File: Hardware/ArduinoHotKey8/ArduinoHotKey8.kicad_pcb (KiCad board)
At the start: 2 copper layers, 96.5 x 77.5 mm, 38 parts, among them SW0 SW_Push, SW1 SW_Push, SW2 SW_Push, SW3 SW_Push, SW4 SW_Push, SW5 SW_Push, SW6 SW_Push, SW7 SW_Push

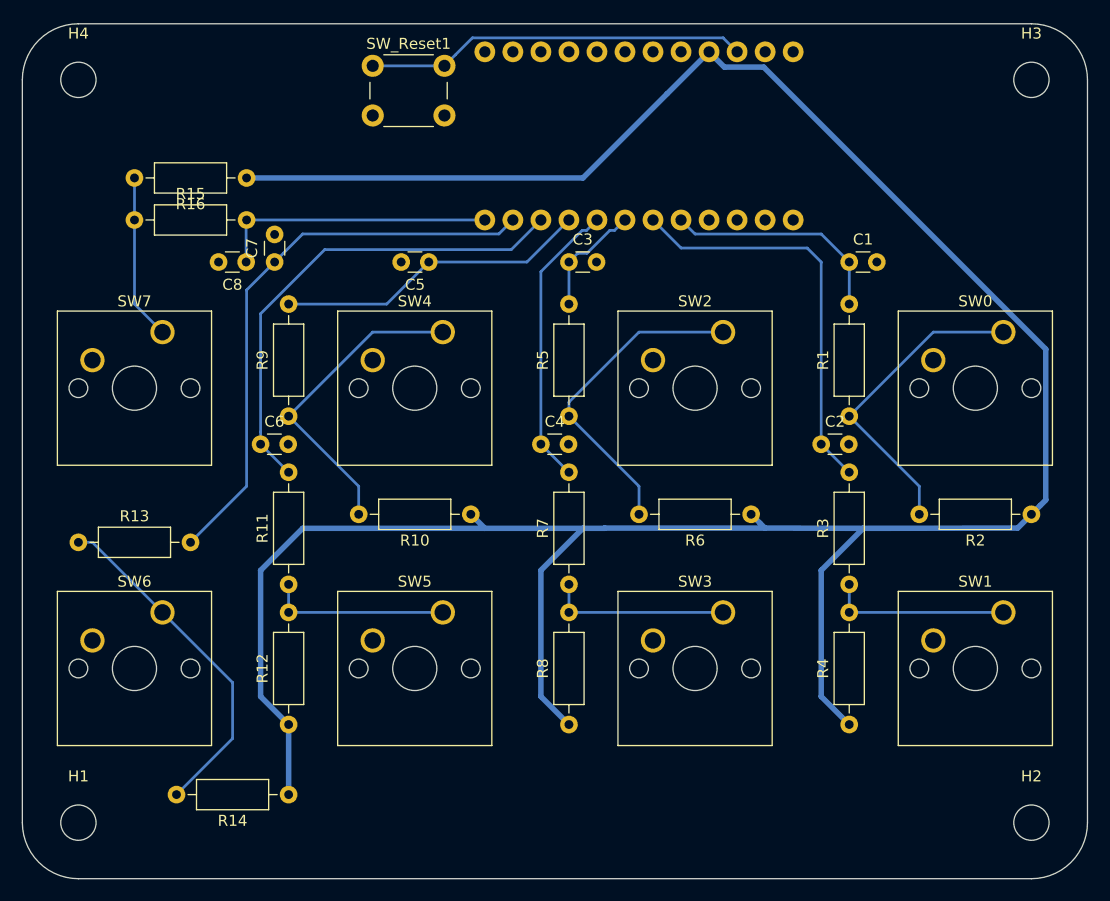
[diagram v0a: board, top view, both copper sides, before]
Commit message: Update ArduinoHotKey8.kicad_pcb
Fixed missing infill
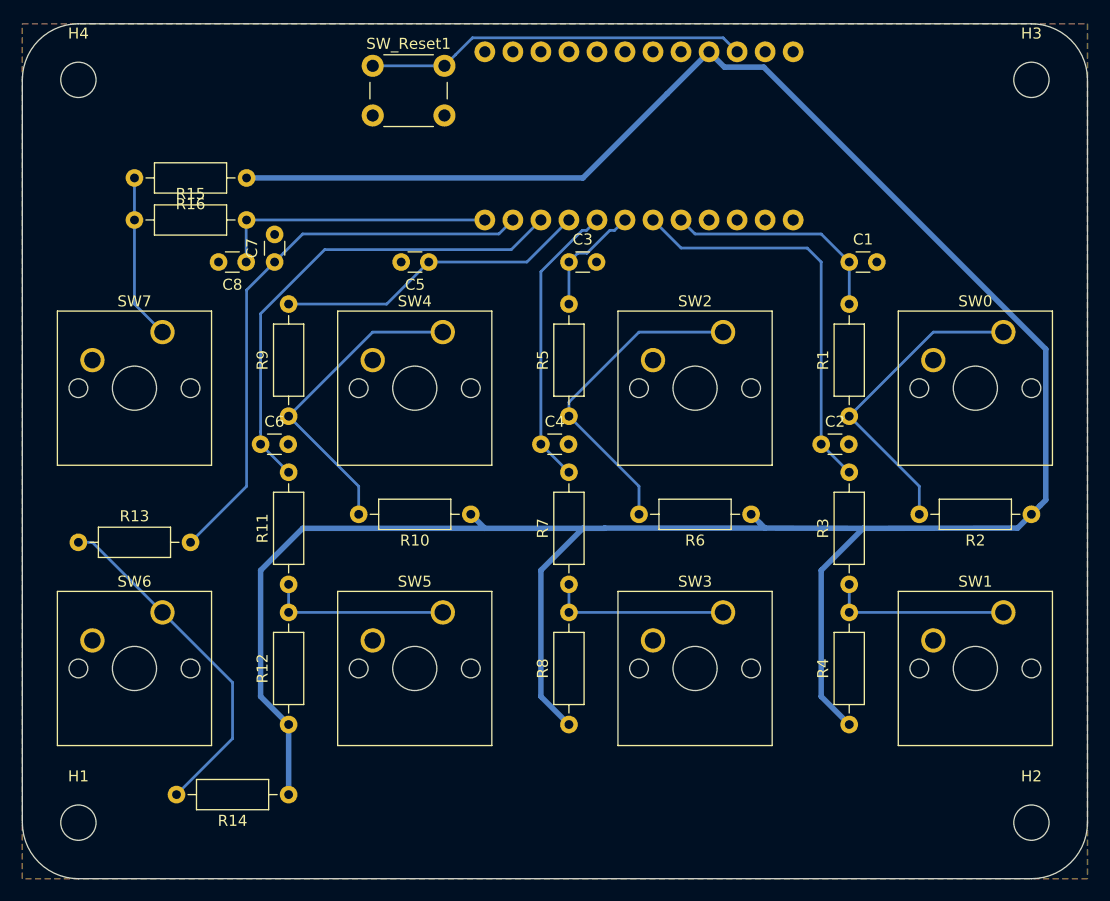
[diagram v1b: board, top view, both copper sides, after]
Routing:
- added copper zone on B.Cu, net GND
- added copper zone on F.Cu, net GND
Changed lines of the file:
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@@
     (solder_mask_min_width 0.25)
     (aux_axis_origin 0 0)
-    (visible_elements FFFFFF7F)
+    (visible_elements 7FFFFFFF)
     (pcbplotparams
       (layerselection 0x010fc_ffffffff)
@@
   (segment (start 30.48 45.72) (end 33.02 48.26) (width 0.25) (layer B.Cu) (net 19))
   (segment (start 30.48 38.1) (end 30.48 45.72) (width 0.25) (layer B.Cu) (net 19))
+  (zone (net 1) (net_name GND) (layer F.Cu) (hatch edge 0.508)
+    (connect_pads (clearance 0.508))
+    (min_thickness 0.254)
+    (fill yes (arc_segments 32) (thermal_gap 0.508) (thermal_bridge_width 0.508))
+    (polygon
+      (pts
+        (xy 116.84 97.79) (xy 20.32 97.79) (xy 20.32 20.32) (xy 116.84 20.32)
+      )
+    )
+  )
+  (zone (net 1) (net_name GND) (layer B.Cu) (hatch edge 0.508)
+    (connect_pads (clearance 0.508))
+    (min_thickness 0.254)
+    (fill yes (arc_segments 32) (thermal_gap 0.508) (thermal_bridge_width 0.508))
+    (polygon
+      (pts
+        (xy 116.84 97.79) (xy 20.32 97.79) (xy 20.32 20.32) (xy 116.84 20.32)
+      )
+    )
+  )
 )

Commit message: Added ISP Header
Added ISP Header and moved bulky parts to the back
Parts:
- added J1: AVR-ISP-6, Connector_IDC:IDC-Header_2x03_P2.54mm_Vertical, B.Cu at (39.4, 25.4)
- SW_Reset1: moved to B.Cu
- moved SW_Reset1 6.35 mm to (58.4, 24.1), turned to 180 degrees
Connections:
- net Net-(B1-Pad22) renamed /RST
- B1 pad 14: (no net) -> /MOSI
- B1 pad 15: (no net) -> /MISO
- B1 pad 16: (no net) -> /SCK
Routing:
- net VCC: track 241.5 -> 293.1 mm
- net /MISO: track 0.00 -> 33.8 mm
- net /SCK: track 0.00 -> 30.0 mm
- net /MOSI: track 0.00 -> 25.0 mm
- net /RST: track 34.6 -> 41.7 mm
- net GND: vias 0 -> 2

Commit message: Update ArduinoHotKey8.kicad_pcb
Added Label
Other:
- board text added: "ArduinoHotKey 8 Buttons V1.0"
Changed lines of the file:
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@@
   (general
     (thickness 1.6)
-    (drawings 8)
+    (drawings 9)
     (tracks 130)
     (zones 0)
@@
     )
   )
+  (gr_text "ArduinoHotKey\n8 Buttons V1.0" (at 68.58 31.75) (layer F.SilkS)
+    (effects (font (size 1 1) (thickness 0.15)))
+  )
   (gr_arc (start 111.76 92.71) (end 111.76 97.79) (angle -90) (layer Edge.Cuts) (width 0.05))
